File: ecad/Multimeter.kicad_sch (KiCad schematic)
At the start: 14 parts, among them J1 Red Banana Plug, J2 Black Banana Plug, SW1 SW_Push_DPDT, U1 SC0915, U3 MCP6001-OT, U4 MCP3561

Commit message: stuff
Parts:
- removed C1, C2, C3: 0.1uF, symbol Device:C
- removed J1: Red Banana Plug, symbol Connector_Generic:Conn_01x01
- removed J2: Black Banana Plug, symbol Connector_Generic:Conn_01x01
- removed R1, R4: R_US, symbol Device:R_US
- removed R2: 10k, symbol Device:R_US
- removed R3, R5: 10k+/-0.1%, symbol Device:R_US
- removed SW1: SW_Push_DPDT, symbol Switch:SW_Push_DPDT
- removed U3: MCP6001-OT, Package_TO_SOT_SMD:SOT-23-5, symbol Amplifier_Operational:MCP6001-OT
- removed U4: MCP3561, symbol multimeter_parts:MCP3561
- added D5: B140-13-F, Diode_SMD:D_0805_2012Metric, symbol Device:D_Schottky
- added D6: D_Zener, symbol Device:D_Zener
- added F1: Fuse, Diode_SMD:D_0805_2012Metric, symbol Device:Fuse
- added J1: USB_B_Micro, symbol Connector:USB_B_Micro
- added TP4, TP5: TestPoint_Alt, symbol Connector:TestPoint_Alt
- U1: footprint SC0915:MODULE_SC0915 -> Multimeter:MODULE_SC0915
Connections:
- net +5V: now also D5.2 (A), D6.1 (K), F1.2, TP5.1
- net GND: now also D6.2 (A), J1.5 (GND), J1.6 (Shield), TP4.1
- net Display/low_ohm: now reaches U1.12 (GP9)
- net Display/micro: now reaches U1.14 (GP10)
- net Display/nano: now reaches U1.15 (GP11)
- net Display/pico: now reaches U1.16 (GP12)
- net Display/CLK: now reaches U1.25 (GP19)
- net Display/SD: now reaches U1.26 (GP20)
- net Display/digit1: now reaches U1.27 (GP21)
- net Display/digit2: now reaches U1.29 (GP22)
- net Display/digit3: now reaches U1.31 (GP26)
- net Display/digit4: now reaches U1.32 (GP27)
- net at U1.39 (VSYS): now also D5.1 (K)
- net Analog Front End/SCK: now reaches U1.4 (GP2)
- net Analog Front End/SDI: now reaches U1.5 (GP3)
- net Analog Front End/SDO: now reaches U1.6 (GP4)
- net Analog Front End/CS: now reaches U1.7 (GP5)
- net Analog Front End/MDAT: now reaches U1.9 (GP6)
- net +3.3V: no longer names the net of U1.36 (3V3_OUT)
- new net: F1.1, J1.1 (VBUS)
- no-connect marks 3 -> 26
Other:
- added sheet Analog Front End (analog_front _end.kicad_sch)
- added sheet Display (display.kicad_sch)
- moved on the sheet: U1

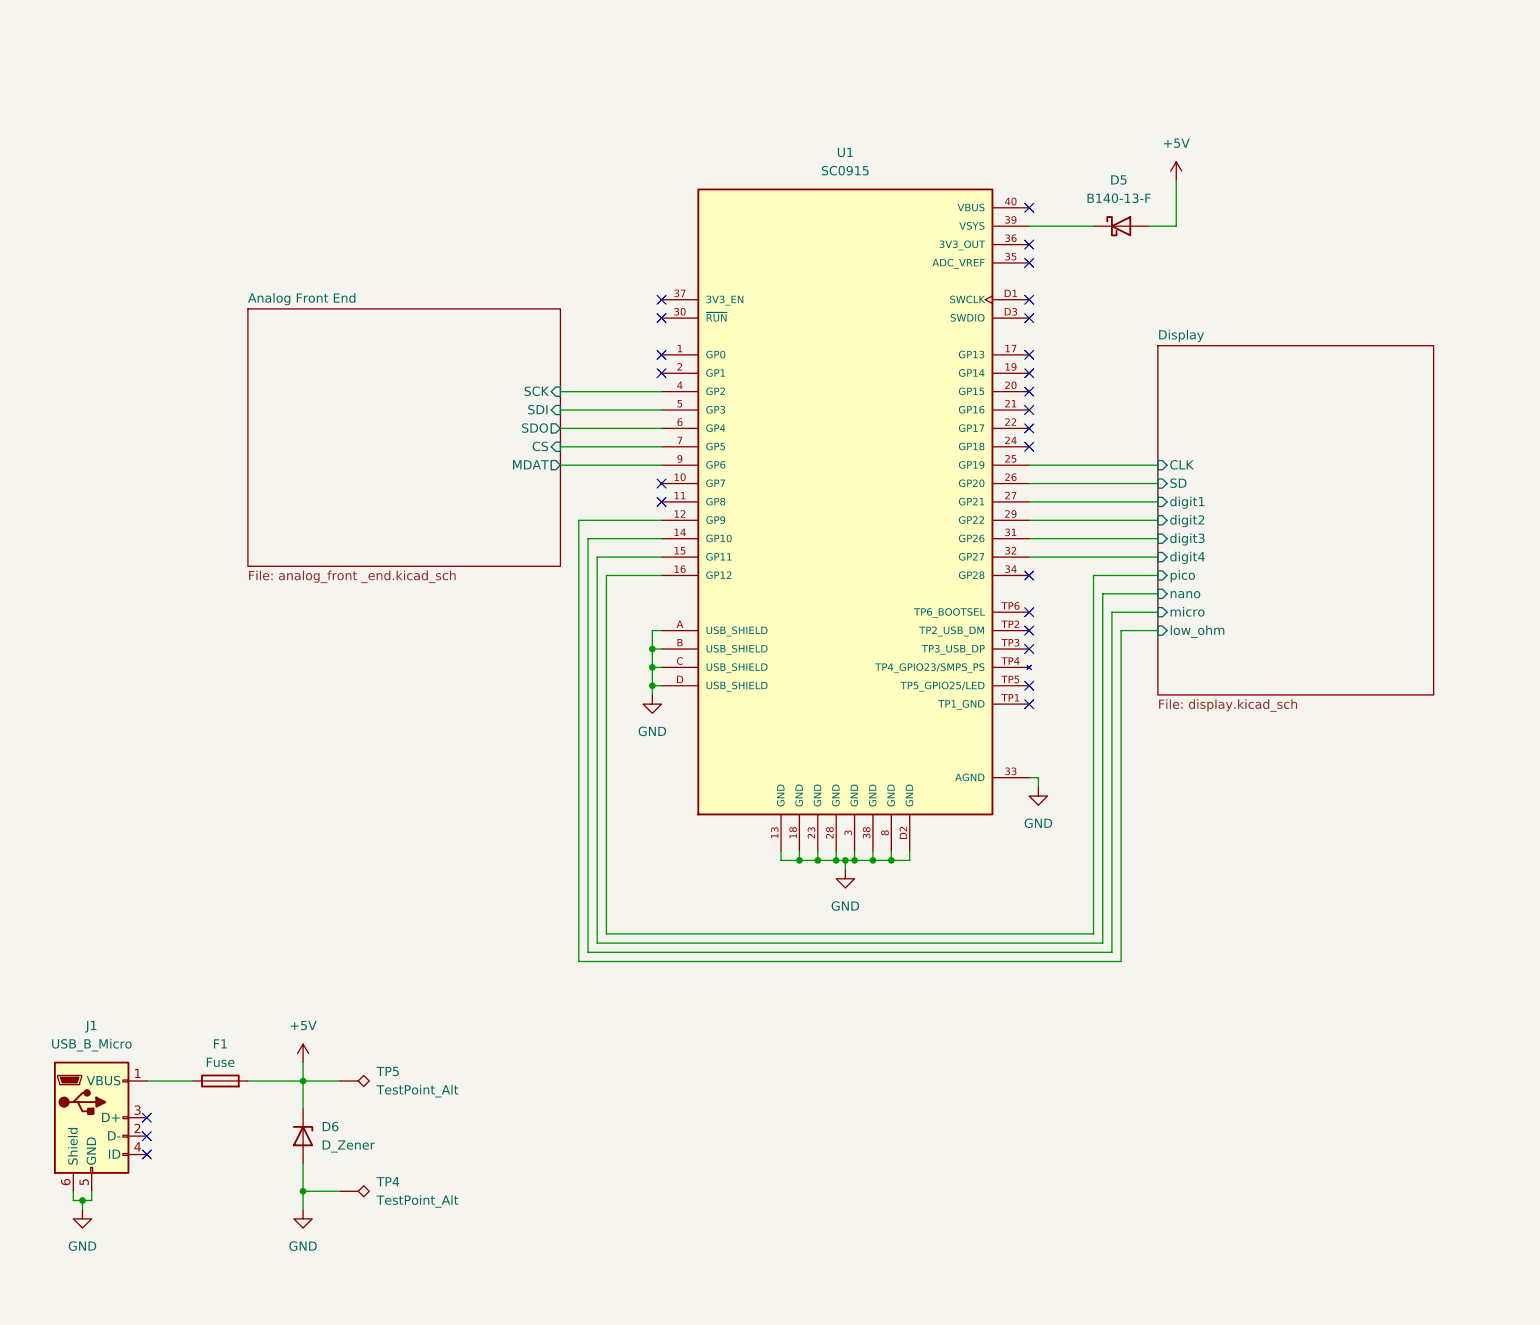
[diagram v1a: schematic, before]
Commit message: cap interpolation test
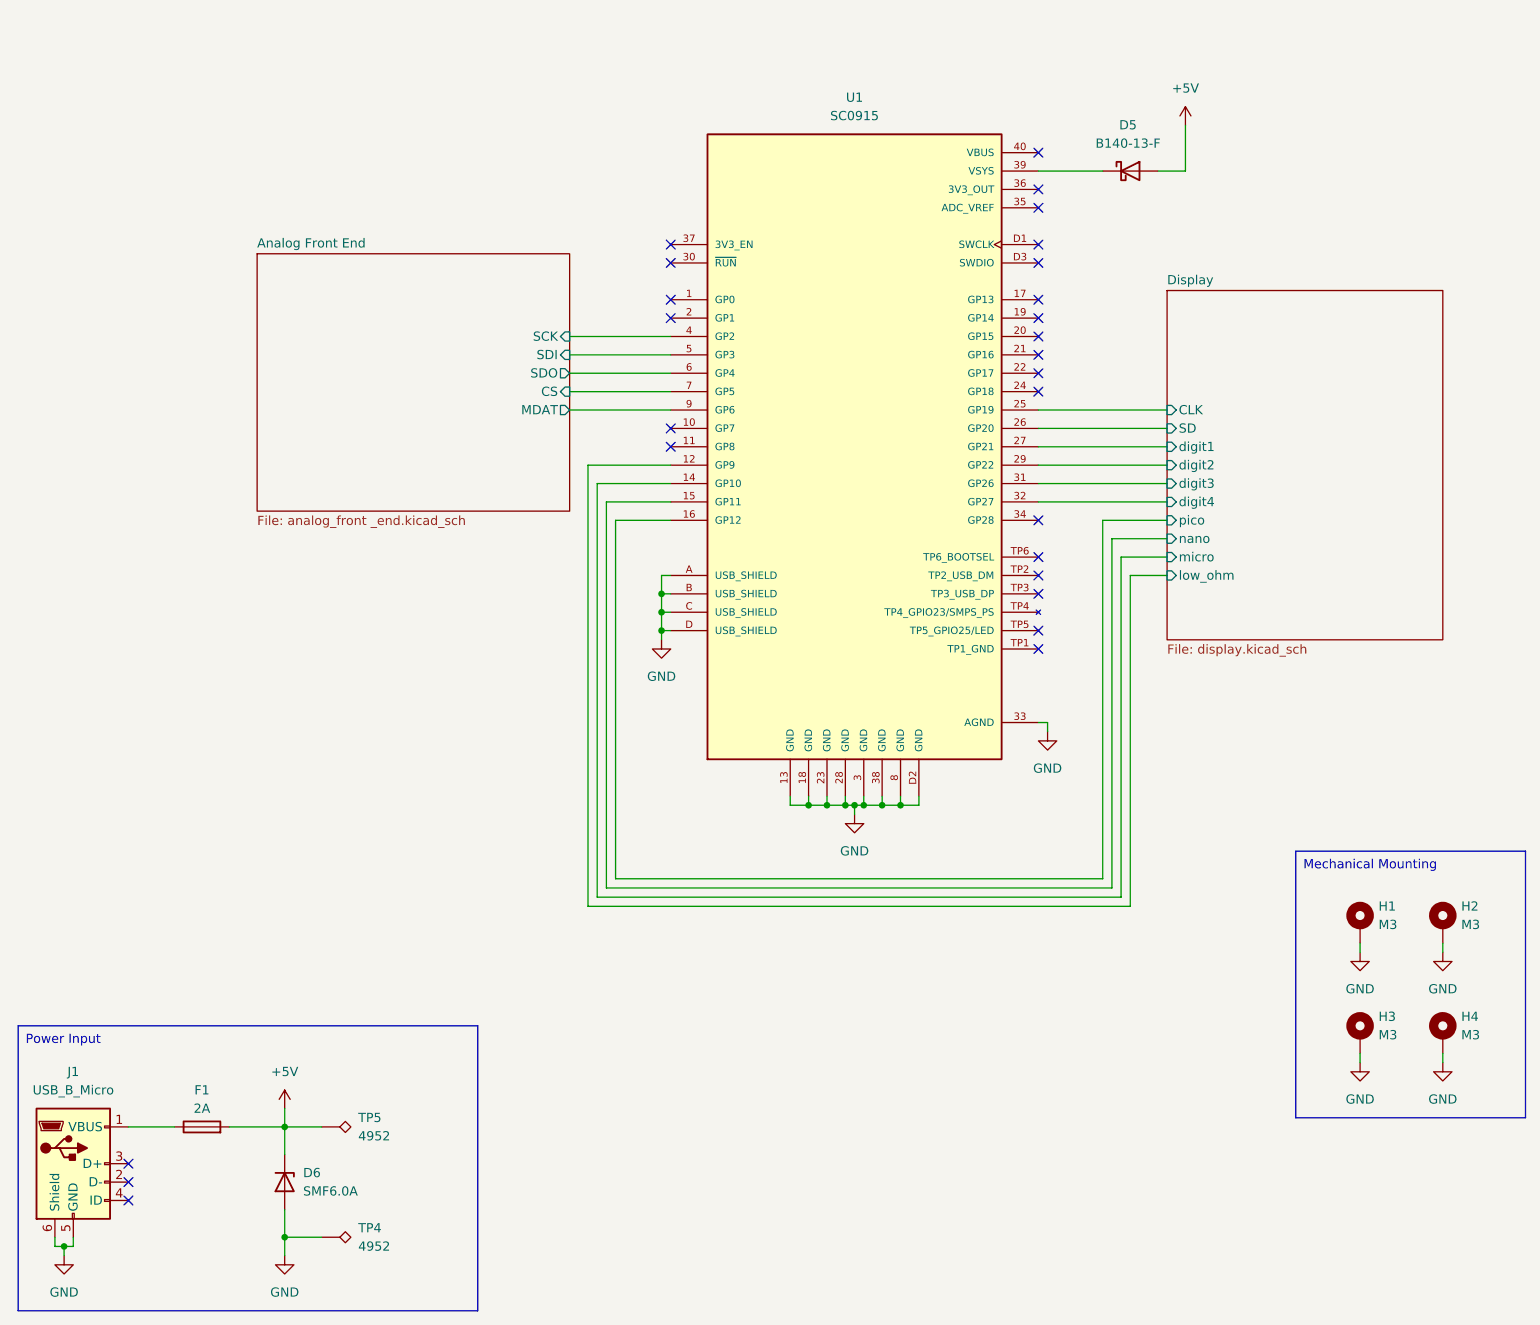
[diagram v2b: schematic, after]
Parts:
- added H1, H2, H3, H4: M3, MountingHole:MountingHole_2.7mm_Pad_Via, symbol Mechanical:MountingHole_Pad
- D6: value D_Zener -> SMF6.0A; footprint (none) -> Diode_SMD:D_SOD-123F
- F1: value Fuse -> 2A
- J1: footprint (none) -> Connector_USB:USB_Micro-AB_Molex_47590-0001
- TP4, TP5: value TestPoint_Alt -> 4952; footprint (none) -> TestPoint:TestPoint_THTPad_1.5x1.5mm_Drill0.7mm
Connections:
- net GND: now also H1.1, H2.1, H3.1, H4.1
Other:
- moved on the sheet: D5, D6, F1, J1, TP4, TP5, U1

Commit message: layout finished
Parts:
- added R3: 10k, Capacitor_SMD:C_0805_2012Metric_Pad1.18x1.45mm_HandSolder, symbol Device:R_US
- added SW1: GF-123-0054, Multimeter:SW_GF-123-0054, symbol Switch:SW_SPST
- D5: Digikey Part # (none) -> B140-FDICT-ND; Part # (none) -> B140-13-F; Unit Price (none) -> 0.39
- D6: Digikey Part # (none) -> F5749CT-ND; Part # (none) -> SMF6.0A; Unit Price (none) -> 0.45
- F1: Digikey Part # (none) -> 2315-FCC20202AATPCT-ND; Part # (none) -> FCC20202AATP; Unit Price (none) -> 0.1
- J1: Digikey Part # (none) -> WM17144CT-ND; Part # (none) -> 0475900001; Unit Price (none) -> 0.86
- TP4, TP5: Digikey Part # (none) -> 36-4952-ND; Part # (none) -> 4952; Unit Price (none) -> 0.26
- U1: Availability In Stock -> (none); Check_prices https://www.snapeda.com/parts/SC0915/Raspberry+Pi/view-part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 -> (none); Digikey Part # (none) -> 2648-SC0915CT-ND; MANUFACTURER Pi Supply -> (none); MF Raspberry Pi -> (none); MP SC0915 -> (none); PARTREV 1.9 -> (none); Package None -> (none); Part # (none) -> SC0915; Price None -> (none); Purchase-URL https://www.snapeda.com/api/url_track_click_mouser/?unipart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 -> (none); SNAPEDA_PN SC0915 -> (none); STANDARD Manufacturer Recommendations -> (none); SnapEDA_Link https://www.snapeda.com/parts/SC0915/Raspberry+Pi/view-part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 -> (none); Unit Price (none) -> 4.00
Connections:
- net GND: now also SW1.1 (A)
- net at U1.2 (GP1): now also R3.2, SW1.2 (B)
- net +3.3V: now reaches U1.36 (3V3_OUT)
- net +3.3V: now also R3.1
- no-connect marks 26 -> 24
